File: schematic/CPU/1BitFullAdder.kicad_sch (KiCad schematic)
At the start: 5 parts, among them U23 74LS86, U24 74LS08, U25 74LS86, U26 74LS08, U27 74LS32

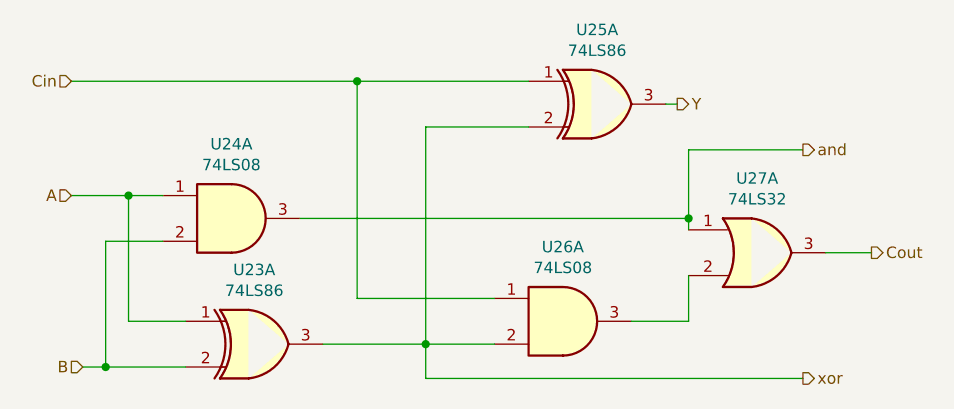
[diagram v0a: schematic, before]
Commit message: ttl fpga: factorization works in sim and fpga
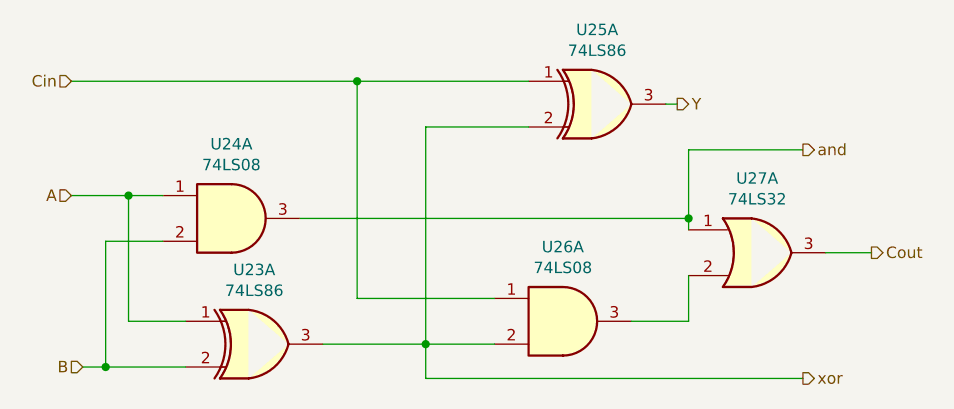
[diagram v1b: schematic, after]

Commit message: alu figures, modules finished
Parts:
- U28: renamed from U23; value 74LS86 -> (none); footprint Package_DIP:DIP-14_W7.62mm -> (none)
- U29: renamed from U24; value 74LS08 -> (none); footprint Package_DIP:DIP-14_W7.62mm -> (none)
- U30: renamed from U25; value 74LS86 -> (none); footprint Package_DIP:DIP-14_W7.62mm -> (none)
- U31: renamed from U26; value 74LS08 -> (none); footprint Package_DIP:DIP-14_W7.62mm -> (none)
- U32: renamed from U27; value 74LS32 -> (none); footprint Package_DIP:DIP-14_W7.62mm -> (none)
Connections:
- net xor is gone; now on net and: U28.3, U30.2, U31.2
